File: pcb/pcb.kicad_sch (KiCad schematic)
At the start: 28 parts, among them IC1 LD1117-3.3V-SOT223, J1 Input, J2 Output, J3 PinHeader_01x05_P2.54mm_Horiz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, SW1 Push_Button

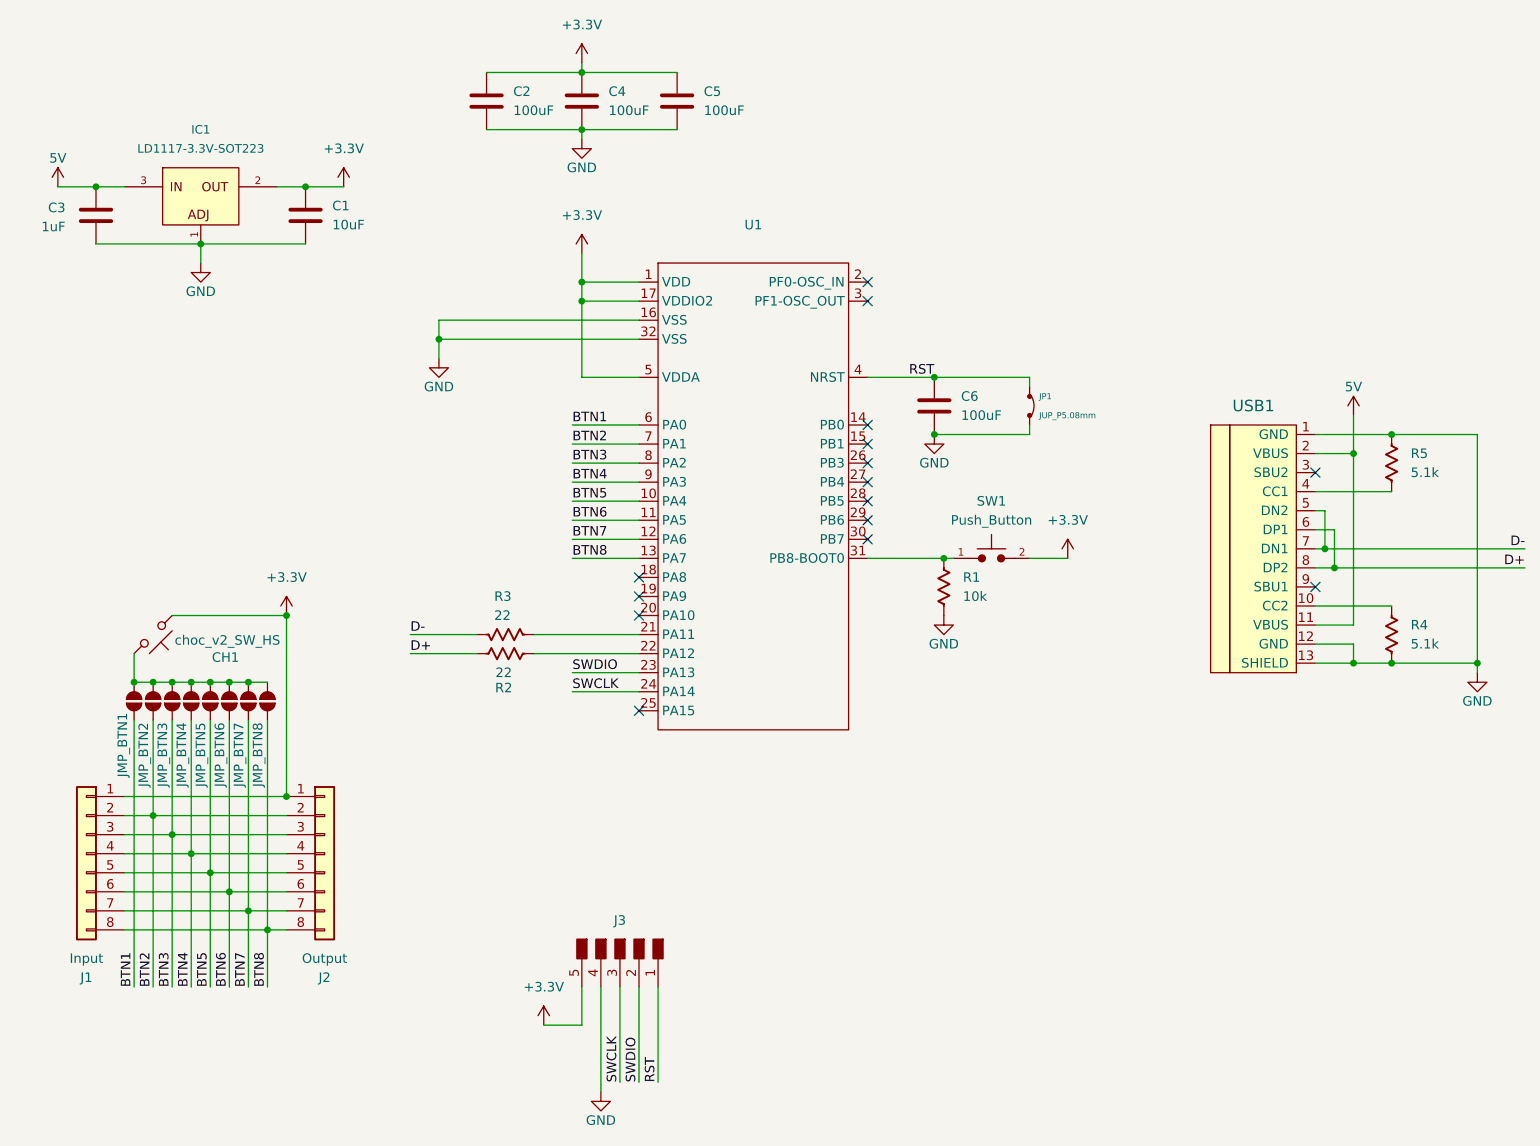
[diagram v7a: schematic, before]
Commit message: revised pcb because im a dummy and put the wrong mcu size
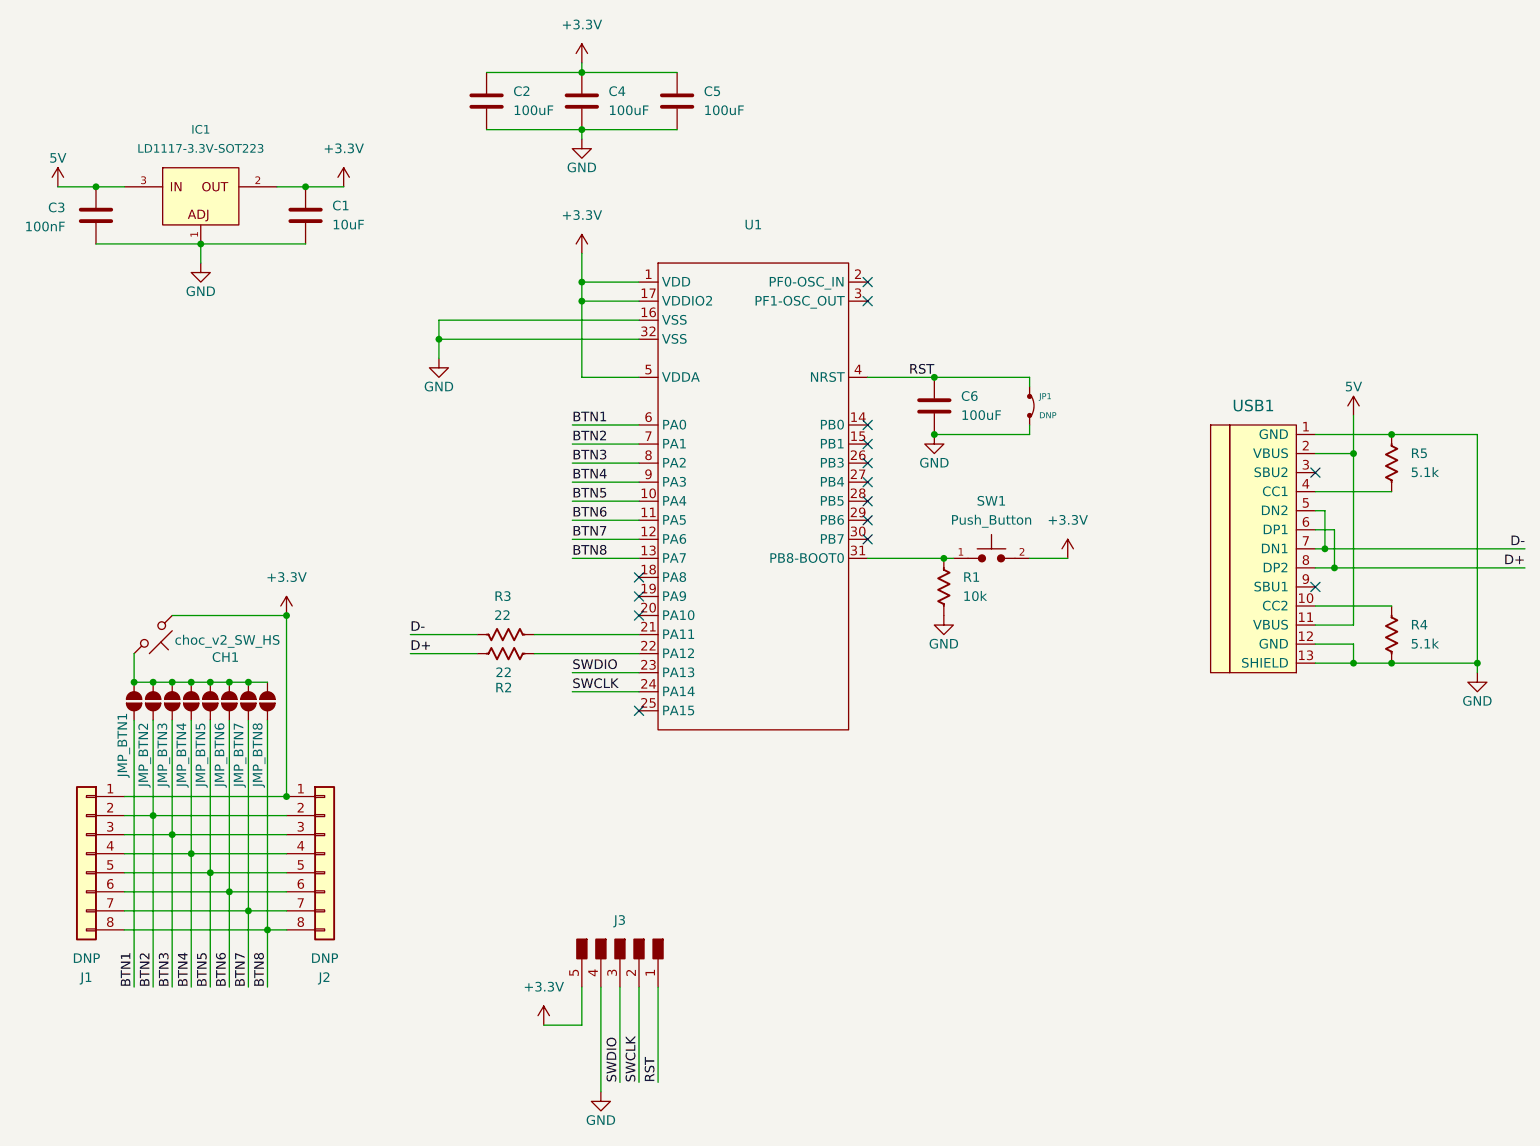
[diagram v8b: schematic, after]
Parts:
- C3: value 1uF -> 100nF
- CH1: footprint PCM_marbastlib-choc:SW_choc_v1_HS_CPG135001S30_1u -> PCM_Switch_Keyboard_Hotswap_Kailh:SW_Hotswap_Kailh_Choc_V1V2
- J1: value Input -> DNP
- J2: value Output -> DNP
- J3: value PinHeader_01x05_P2.54mm_Horizontal_SMD -> DNP
- JP1: value JUP_P5.08mm -> DNP
- U1: footprint PCM_Package_QFP_AKL:LQFP-36_7x7mm_P0.65mm -> PCM_Package_QFP_AKL:LQFP-32_7x7mm_P0.8mm
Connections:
- net SWCLK: now also J3.2 (Pin_2); no longer J3.3 (Pin_3)
- net SWDIO: now also J3.3 (Pin_3); no longer J3.2 (Pin_2)
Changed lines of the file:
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@@
+		)
+	)
+	(label "SWCLK"
+		(at 107.95 163.83 90)
+		(effects
+			(font
+				(size 1.27 1.27)
+			)
+			(justify left bottom)
 		)
 	)
@@
 		)
 	)
-	(label "SWCLK"
-		(at 105.41 163.83 90)
-		(effects
-			(font
-				(size 1.27 1.27)
-			)
-			(justify left bottom)
-		)
-	)
 	(label "D-"
 		(at 77.47 104.14 0)
@@
 		)
 	)
+	(label "SWDIO"
+		(at 105.41 163.83 90)
+		(effects
+			(font
+				(size 1.27 1.27)
+			)
+			(justify left bottom)
+		)
+	)
 	(label "BTN5"
 		(at 50.8 151.13 90)
@@
 		)
 	)
-	(label "SWDIO"
-		(at 107.95 163.83 90)
-		(effects
-			(font
-				(size 1.27 1.27)
-			)
-			(justify left bottom)
-		)
-	)
 	(label "BTN2"
 		(at 99.06 78.74 0)
@@
 			)
 		)
-		(property "Value" "PinHeader_01x05_P2.54mm_Horizontal_SMD"
+		(property "Value" "DNP"
 			(at 105.41 142.24 90)
 			(effects
@@
 			)
 		)
-		(property "Value" "Input"
+		(property "Value" "DNP"
 			(at 34.29 147.32 0)
 			(effects
@@
 			)
 		)
-		(property "Value" "1uF"
+		(property "Value" "100nF"
 			(at 31.496 49.7839 0)
 			(effects
@@
 			)
 		)
-		(property "Value" "Output"
+		(property "Value" "DNP"
 			(at 66.04 147.32 0)
 			(effects
@@
 			)
 		)
-		(property "Footprint" "PCM_marbastlib-choc:SW_choc_v1_HS_CPG135001S30_1u"
+		(property "Footprint" "PCM_Switch_Keyboard_Hotswap_Kailh:SW_Hotswap_Kailh_Choc_V1V2"
 			(at 43.18 104.14 0)
 			(effects
@@
 			)
 		)
-		(property "Value" "JUP_P5.08mm"
+		(property "Value" "DNP"
 			(at 161.29 74.93 90)
 			(effects
@@
 			)
 		)
-		(property "Footprint" "PCM_Package_QFP_AKL:LQFP-36_7x7mm_P0.65mm"
+		(property "Footprint" "PCM_Package_QFP_AKL:LQFP-32_7x7mm_P0.8mm"
 			(at 123.19 83.82 0)
 			(effects
